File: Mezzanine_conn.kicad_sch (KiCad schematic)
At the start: 0 parts

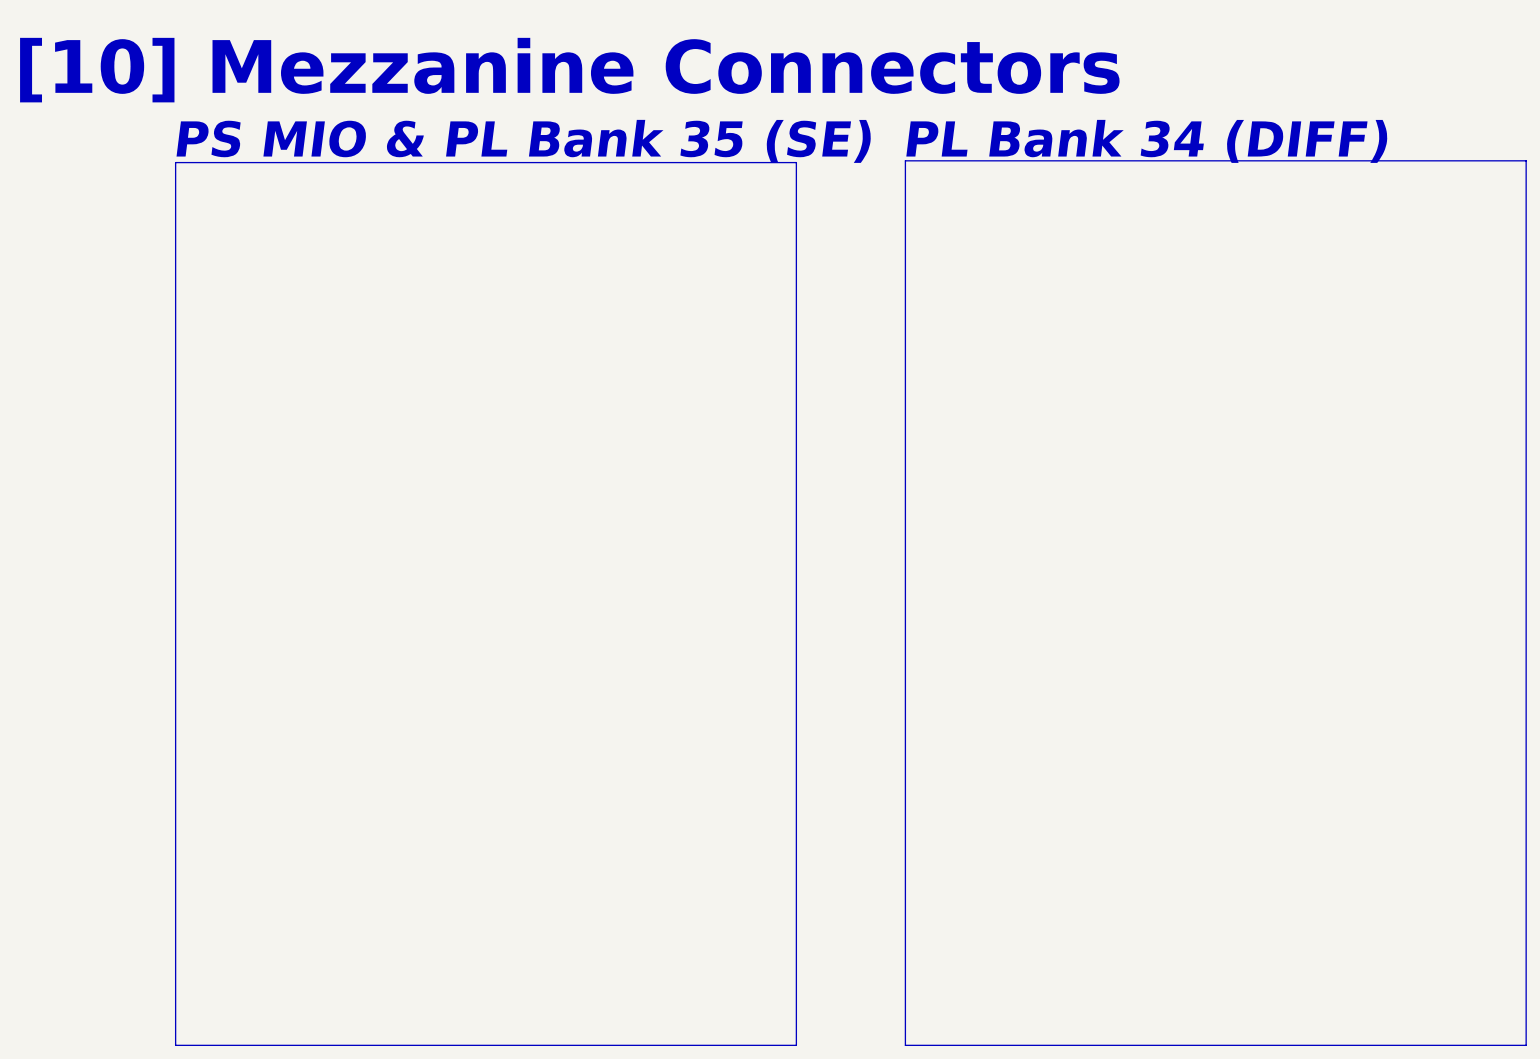
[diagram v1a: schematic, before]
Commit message: Finished first pass of schematic, needs netclass assignments and double check
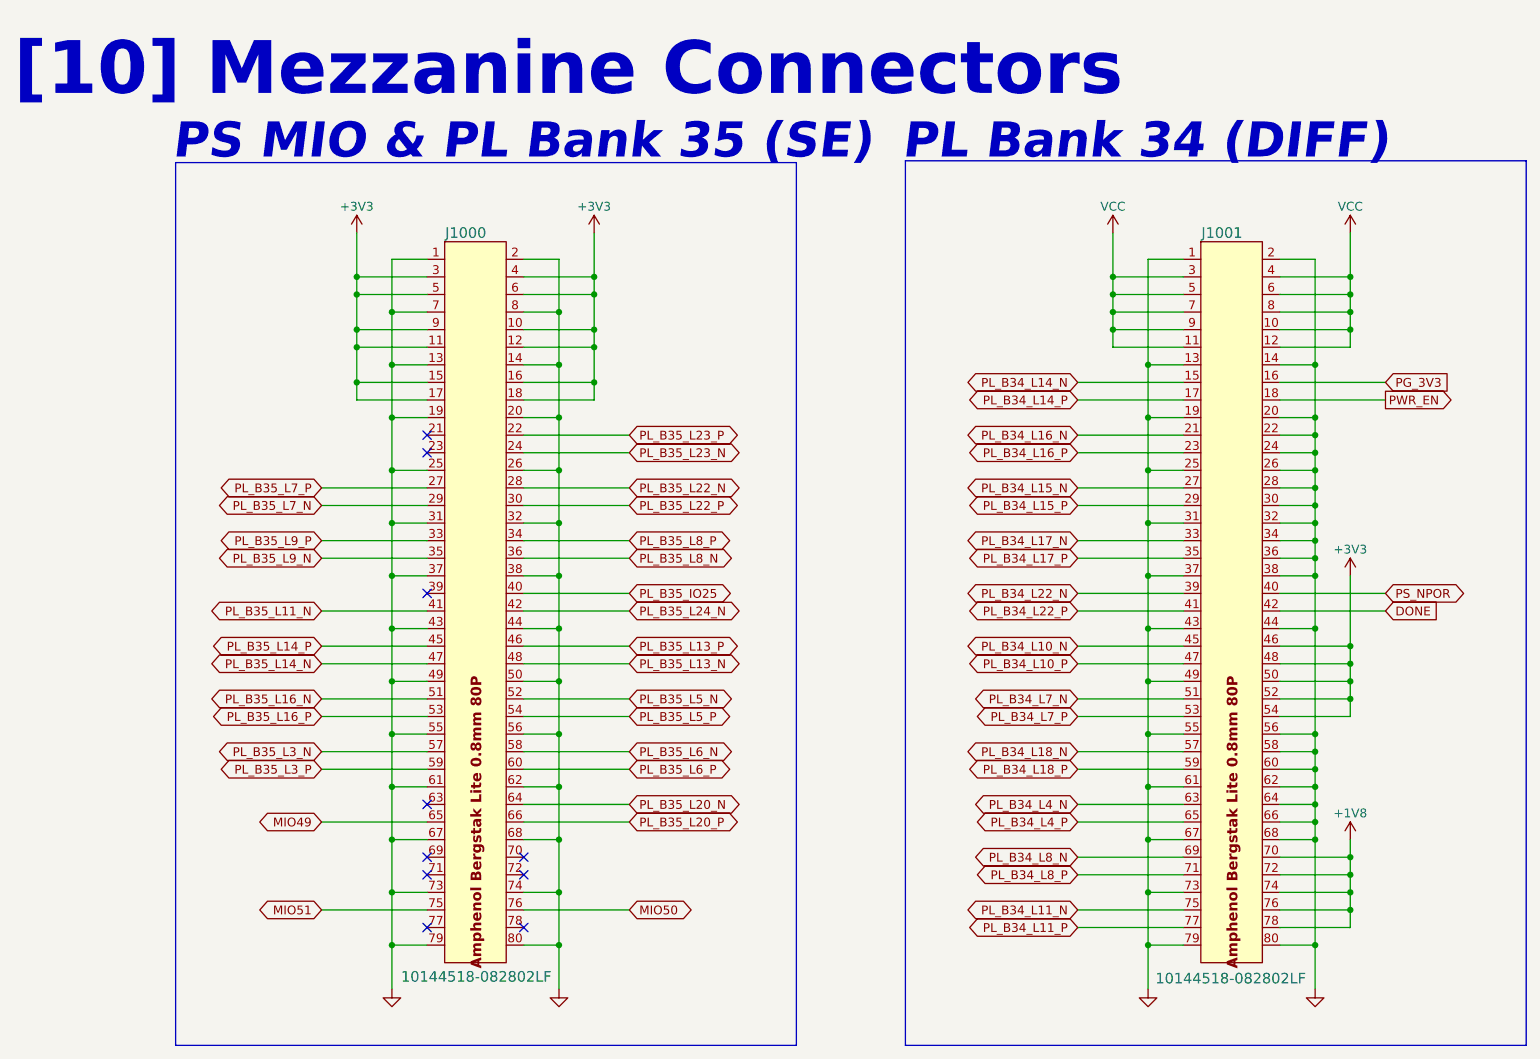
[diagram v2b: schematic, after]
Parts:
- added J1000, J1001: 10144518-082802LF, ZeBra_footprints:CONN_10144518_AMP, symbol ZeBra-X:10144518-082802LF
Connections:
- new net +1V8: J1001.70, J1001.72, J1001.74, J1001.76, J1001.78
- new net +3V3: J1000.10, J1000.11, J1000.12, J1000.15, J1000.16, J1000.17, J1000.18, J1000.3, J1000.4, J1000.5, J1000.6, J1000.9, J1001.46, J1001.48, J1001.50, J1001.52, J1001.54
- new net DONE: J1001.42
- new net GND: J1000.1, J1000.13, J1000.14, J1000.19, J1000.2, J1000.20, J1000.25, J1000.26, J1000.31, J1000.32, J1000.37, J1000.38, J1000.43, J1000.44, J1000.49, J1000.50, J1000.55, J1000.56, J1000.61, J1000.62, J1000.67, J1000.68, J1000.7, J1000.73, J1000.74, J1000.79, J1000.8, J1000.80, J1001.1, J1001.13, J1001.14, J1001.19, J1001.2, J1001.20, J1001.22, J1001.24, J1001.25, J1001.26, J1001.28, J1001.30, J1001.31, J1001.32, J1001.34, J1001.36, J1001.37, J1001.38, J1001.43, J1001.44, J1001.49, J1001.55, J1001.56, J1001.58, J1001.60, J1001.61, J1001.62, J1001.64, J1001.66, J1001.67, J1001.68, J1001.73, J1001.79, J1001.80
- new net MIO49: J1000.65
- new net MIO50: J1000.76
- new net MIO51: J1000.75
- new net PG_3V3: J1001.16
- new net PL_B34_L10_N: J1001.45
- new net PL_B34_L10_P: J1001.47
- new net PL_B34_L11_N: J1001.75
- new net PL_B34_L11_P: J1001.77
- new net PL_B34_L14_N: J1001.15
- new net PL_B34_L14_P: J1001.17
- new net PL_B34_L15_N: J1001.27
- new net PL_B34_L15_P: J1001.29
- new net PL_B34_L16_N: J1001.21
- new net PL_B34_L16_P: J1001.23
- new net PL_B34_L17_N: J1001.33
- new net PL_B34_L17_P: J1001.35
- new net PL_B34_L18_N: J1001.57
- new net PL_B34_L18_P: J1001.59
- new net PL_B34_L22_N: J1001.39
- new net PL_B34_L22_P: J1001.41
- new net PL_B34_L4_N: J1001.63
- new net PL_B34_L4_P: J1001.65
- new net PL_B34_L7_N: J1001.51
- new net PL_B34_L7_P: J1001.53
- new net PL_B34_L8_N: J1001.69
- new net PL_B34_L8_P: J1001.71
- new net PL_B35_IO25: J1000.40
- new net PL_B35_L11_N: J1000.41
- new net PL_B35_L13_N: J1000.48
- new net PL_B35_L13_P: J1000.46
- new net PL_B35_L14_N: J1000.47
- new net PL_B35_L14_P: J1000.45
- new net PL_B35_L16_N: J1000.51
- new net PL_B35_L16_P: J1000.53
- new net PL_B35_L20_N: J1000.64
- new net PL_B35_L20_P: J1000.66
- new net PL_B35_L22_N: J1000.28
- new net PL_B35_L22_P: J1000.30
- new net PL_B35_L23_N: J1000.24
- new net PL_B35_L23_P: J1000.22
- new net PL_B35_L24_N: J1000.42
- new net PL_B35_L3_N: J1000.57
- new net PL_B35_L3_P: J1000.59
- new net PL_B35_L5_N: J1000.52
- new net PL_B35_L5_P: J1000.54
- new net PL_B35_L6_N: J1000.58
- new net PL_B35_L6_P: J1000.60
- new net PL_B35_L7_N: J1000.29
- new net PL_B35_L7_P: J1000.27
- new net PL_B35_L8_N: J1000.36
- new net PL_B35_L8_P: J1000.34
- new net PL_B35_L9_N: J1000.35
- new net PL_B35_L9_P: J1000.33
- new net PS_NPOR: J1001.40
- new net PWR_EN: J1001.18
- new net VCC: J1001.10, J1001.11, J1001.12, J1001.3, J1001.4, J1001.5, J1001.6, J1001.7, J1001.8, J1001.9
- no-connect marks 0 -> 10
